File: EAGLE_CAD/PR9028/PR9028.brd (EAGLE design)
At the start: 65.9 x 66 mm, 60 parts, among them SW1 C&K_PTS645, T1 TPTP20R, T10 TPTP20R, T11 TPTP20R, T12 TPTP20R, T13 TPTP20R, T14 TPTP20R, T15 TPTP20R, T16 TPTP20R, T17 TPTP20R, T2 TPTP20R, T3 TPTP20R, T4 TPTP20R, T5 TPTP20R, T6 TPTP20R, T7 TPTP20R, T8 TPTP20R, T9 TPTP20R, U1 FMIC

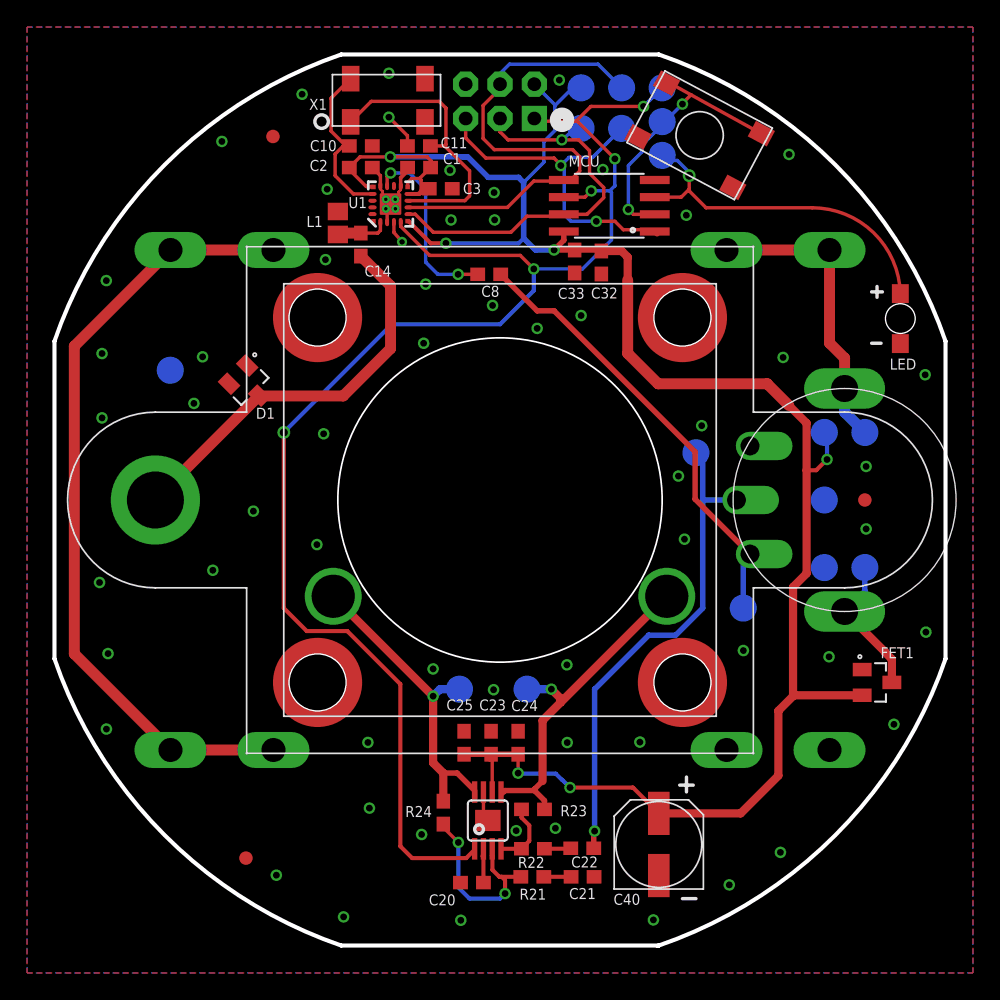
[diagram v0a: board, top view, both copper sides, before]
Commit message: started edits for pot, battery clips
bumping to PR9028. not done with my changes yet, but started.
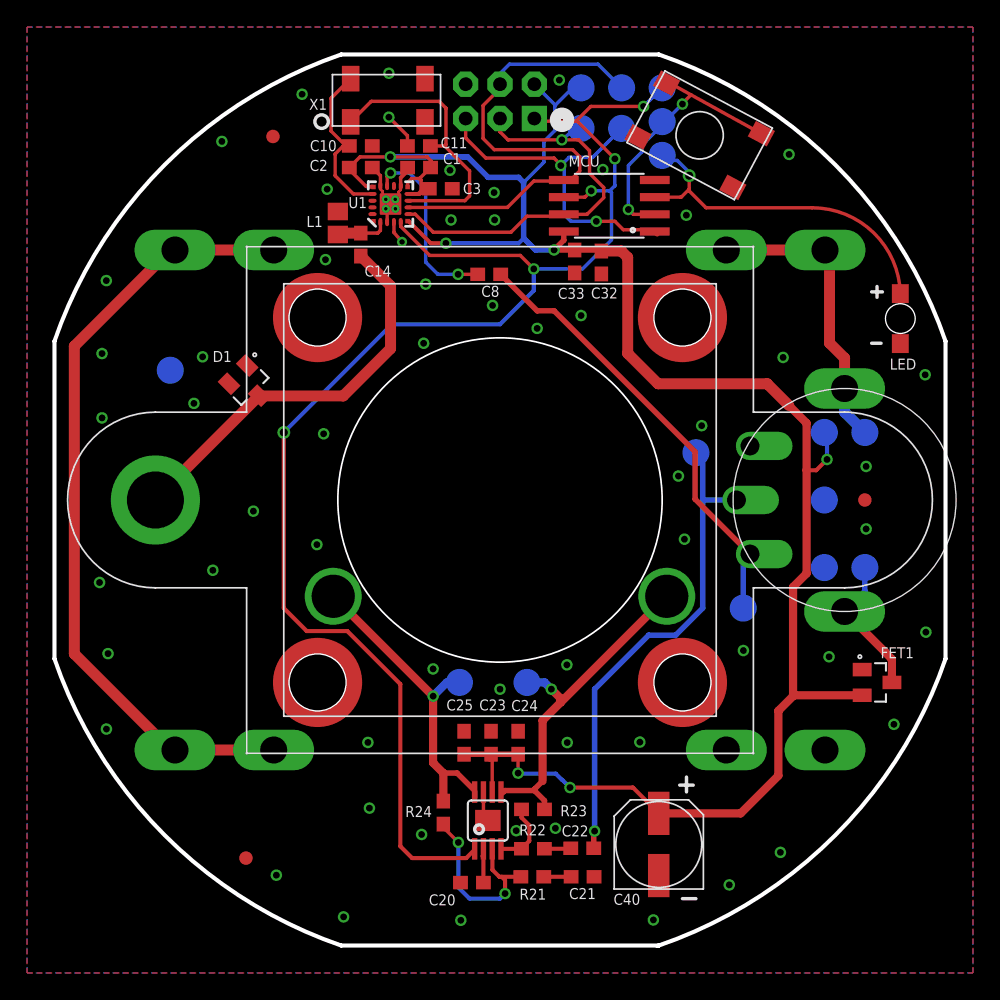
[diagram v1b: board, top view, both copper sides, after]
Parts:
- JP5, JP6: value (none) -> BK-92_MPD_AA_BATT_CLIP
- moved T6 0.50 mm to (37.0, 21.5)
- moved T7 0.50 mm to (32.0, 21.5)

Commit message: updated pot and battery clips
plus small stuff.
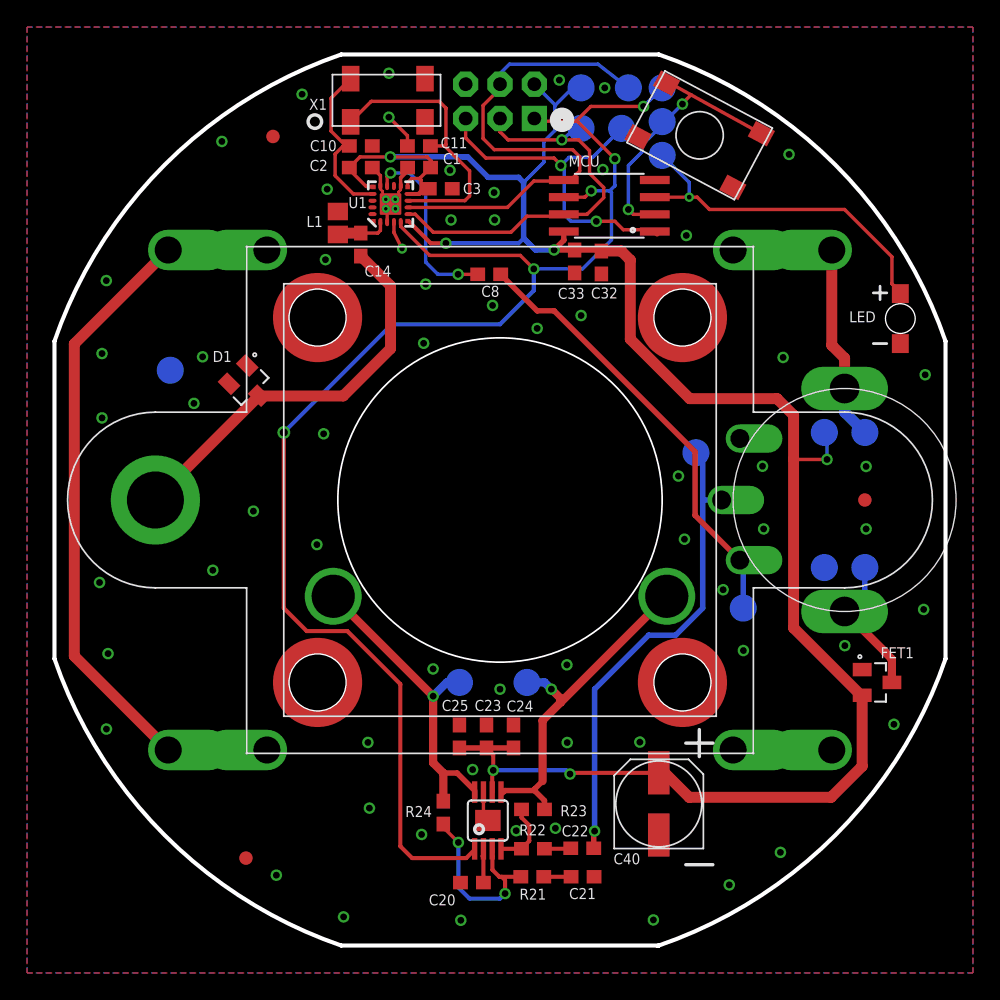
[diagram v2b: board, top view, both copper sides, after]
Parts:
- removed T3: TPTP20R, PR_Parts_Library:TP20R
- moved T2 5.00 mm to (59.0, 30.0)
- moved C40 3.00 mm to (46.8, 12.5)
- moved C23 0.57 mm to (34.0, 17.5)
- moved C24 0.57 mm to (36.0, 17.5)
- moved C25 0.57 mm to (32.0, 17.5)
- moved T13 0.50 mm to (44.5, 65.5)
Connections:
- net GND: no longer T3.TP
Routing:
- net A_OUT: track 36.5 -> 35.4 mm
- net LED/PB4: track 25.4 -> 26.5 mm
- net N$13: track 58.1 -> 57.4 mm
- net GND: track 15.1 -> 15.5 mm, vias 63 -> 67

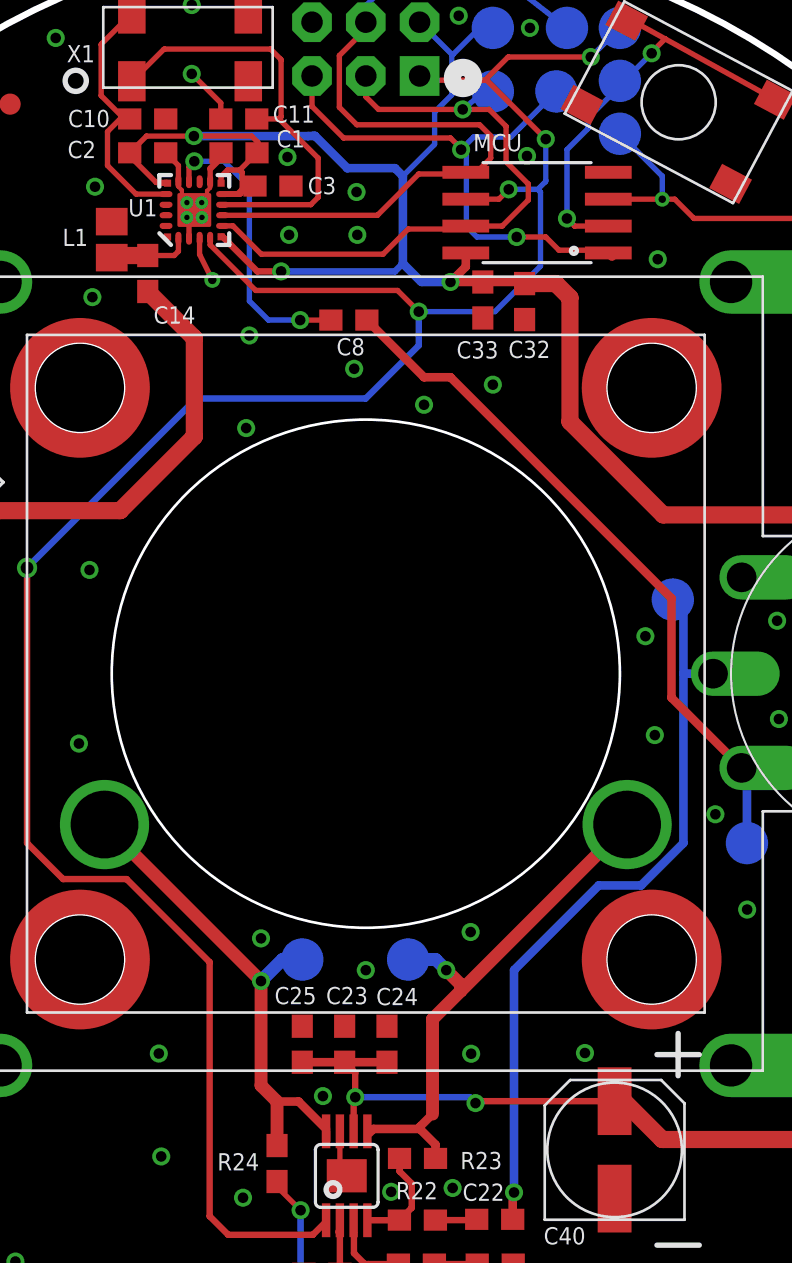
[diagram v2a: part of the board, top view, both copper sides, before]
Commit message: Added jumper footprints
Added back in 0603 footprints for jumpers or potentially ferrite beads:
-L2 near the FMIC required rerouting of the power traces to decoupling caps.
-L3 is near the AMP.
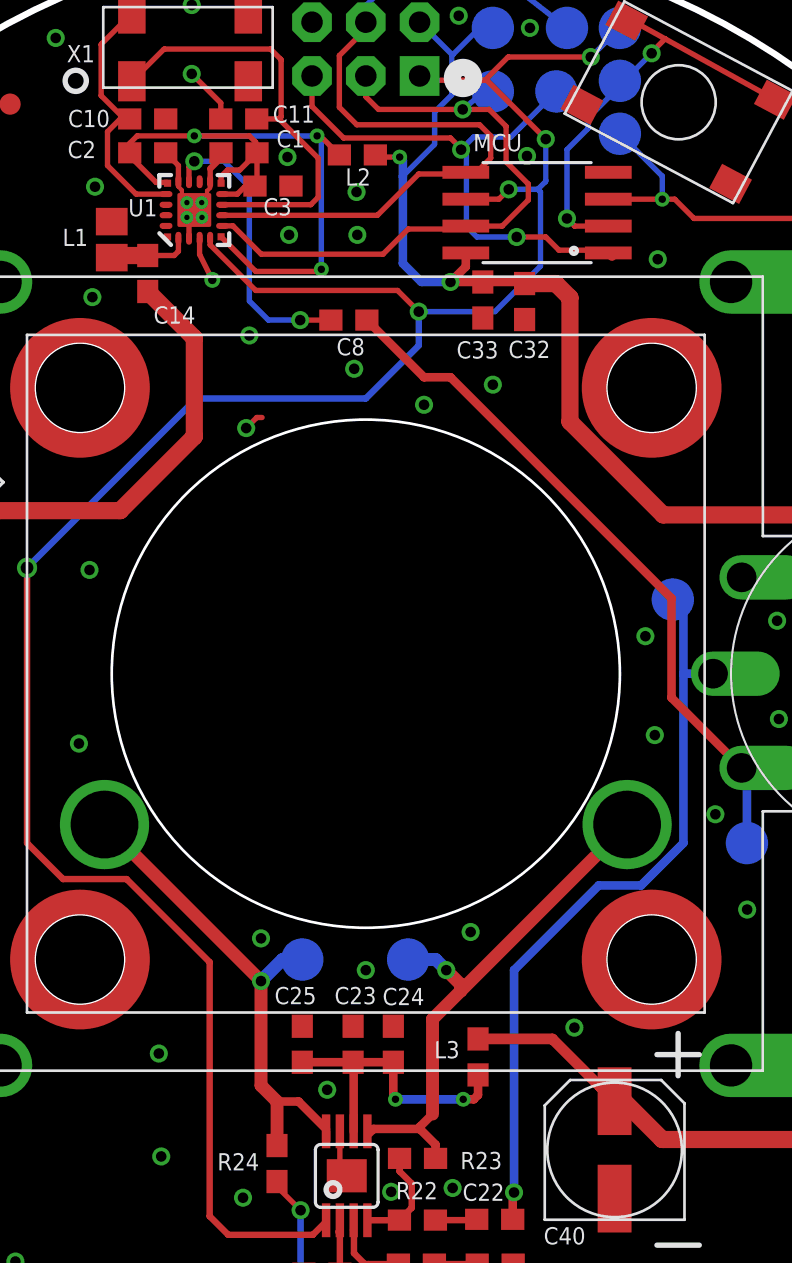
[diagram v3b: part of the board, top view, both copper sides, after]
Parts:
- added L2, L3: 2.2K @ 100Mhz, PR_Parts_Library:0603_CPL
- moved C23 0.40 mm to (34.4, 17.5)
- moved C24 0.30 mm to (36.3, 17.5)
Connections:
- new net N$4: AMP.6, C23.1, C24.1, C25.1, L3.2
- new net N$6: C1.1, C2.1, C3.1, L2.2, U1.10, U1.11, U1.16, U1.6
- net VCC: now also L2.1, L3.1; no longer AMP.6, C1.1, C2.1, C23.1, C24.1, C25.1, C3.1, U1.10, U1.11, U1.16, U1.6
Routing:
- net VCC: track 151.6 -> 106.2 mm, vias 6 -> 3
- net N$6: track 0.00 -> 34.5 mm, vias 0 -> 3
- net N$4: track 0.00 -> 14.3 mm, vias 0 -> 2
- net GND: track 15.5 -> 16.3 mm, vias 67 -> 66
- net LED/PB4: track 26.5 -> 27.0 mm

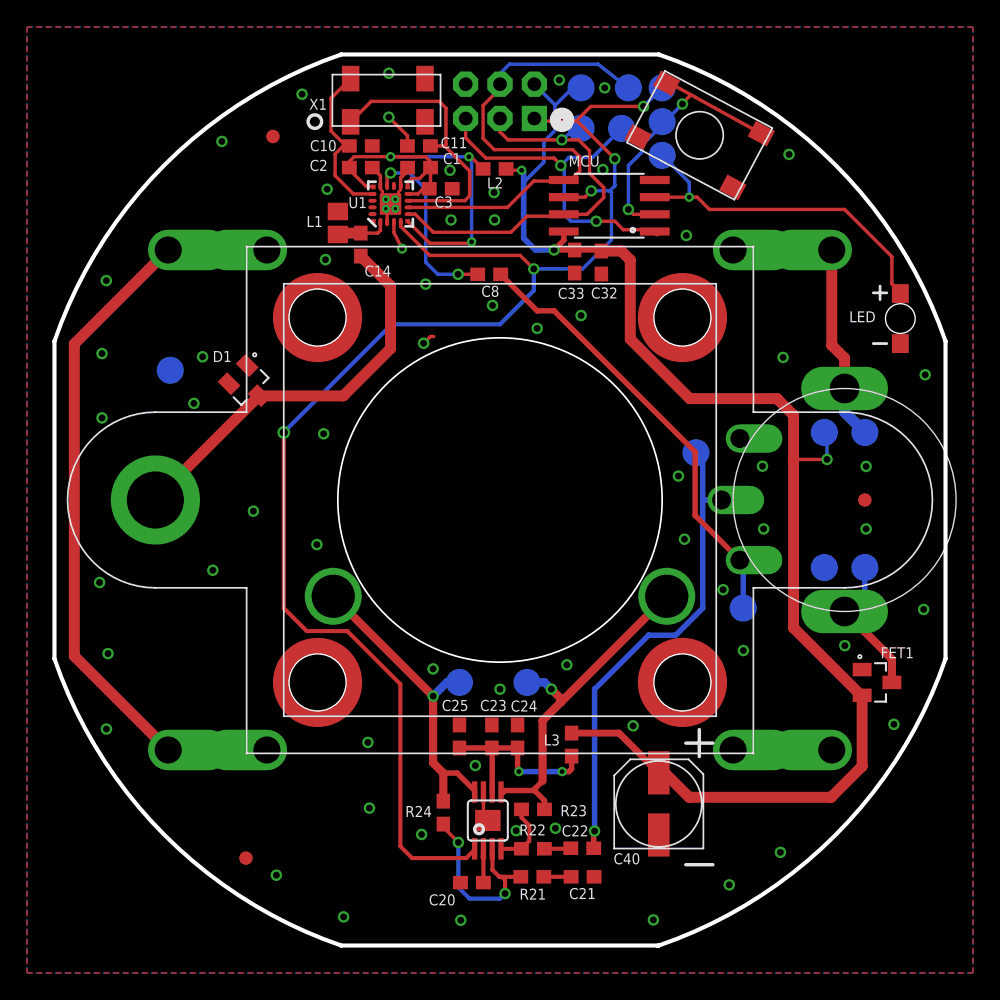
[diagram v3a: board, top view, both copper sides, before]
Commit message: PR9028 Updates
Updated Speaker PEM Nuts:
- currently designed with top and bottom smd pads
- top pad 6.6 mm bottom pad 4.72 mm, drill 4.22 mm
Updated library:
- there are now 3 PEM nut ‘devices:’ ANT, SPK, SPK_GROUND to match our
three different PEM nut uses.
- there are now 2 PEM nut ‘packages:’ ANT, SPK
Updated layout:
- minor changes to some vias
- updated logo placement and URL
Exported BOM & Gerbers
Ran DRC:
- showing errors for speaker Pem nuts & speaker pc pins. need to
confirm with WAI about plating *all* pem nut holes.
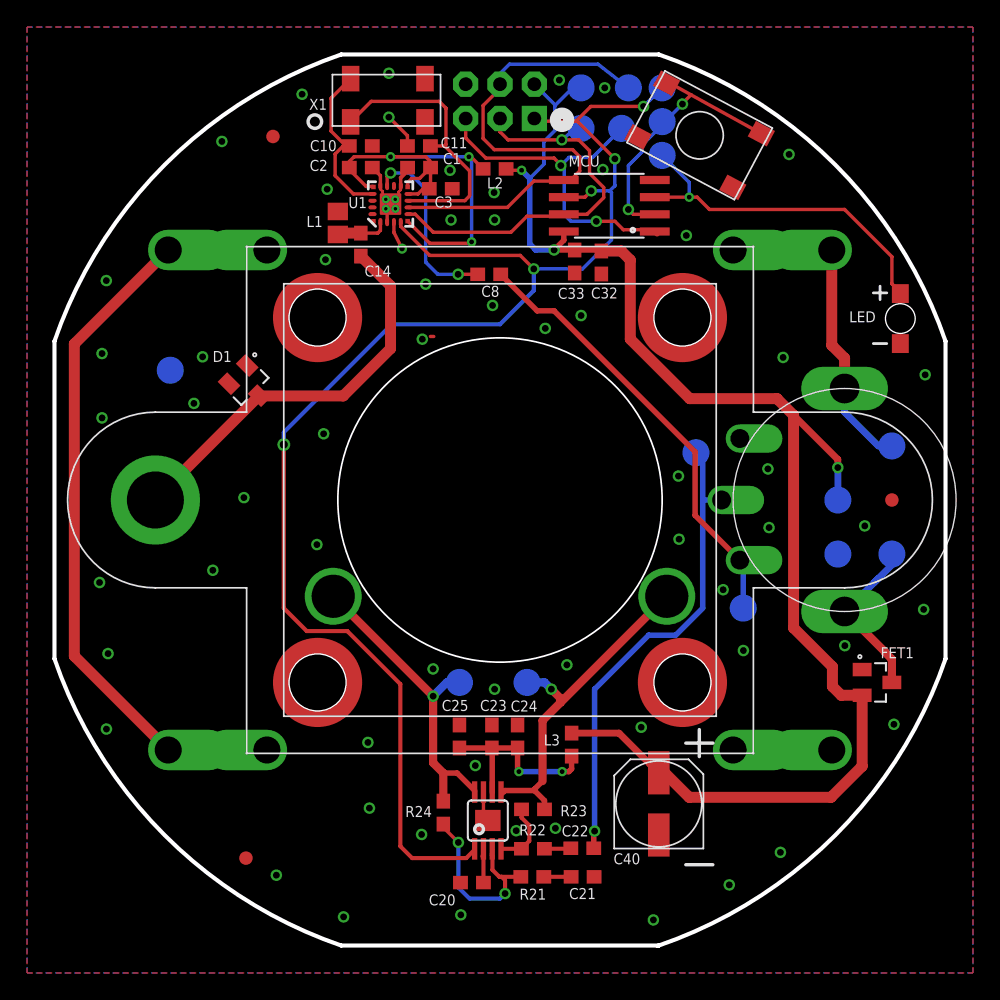
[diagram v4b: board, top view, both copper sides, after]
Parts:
- SPEAKER_PEM_1, SPEAKER_PEM_2, SPEAKER_PEM_4: value PEM_M3_ONE_SIDE -> PEM_M3_SPK; device PR_Parts_Library:PEM_M3_ONE_SIDE -> PR_Parts_Library:PEM_M3_SPK
- SPEAKER_PEM_3: value PEM_M3_ONE_SIDE_W/PIN -> PEM_M3_SPK_GROUND; device PR_Parts_Library:PEM_M3_ONE_SIDE -> PR_Parts_Library:PEM_M3_SPK
- moved T4 5.10 mm to (60.0, 35.0)
- moved T14 2.24 mm to (64.0, 31.0)
- moved T15 2.24 mm to (64.0, 39.0)
- moved MARK3 2.00 mm to (64.0, 35.0)
- moved T2 1.41 mm to (60.0, 31.0)
- moved U$1 0.40 mm to (35.0, 8.60)
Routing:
- net VCC: track 106.2 -> 110.0 mm
- net SW_OUT: track 21.8 -> 24.2 mm
- net SW_IN: track 10.6 -> 12.8 mm
- net GND: track 16.3 -> 15.6 mm, vias 66 -> 65
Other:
- board text added: "www.thepublicrad.io"
- board text removed: "The Public Radio Born in Brooklyn http://thepublicrad.io"

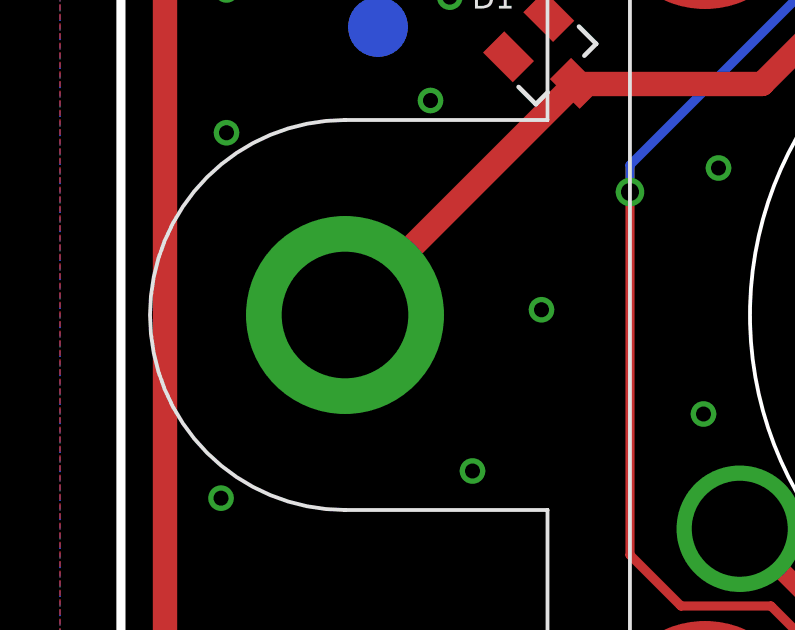
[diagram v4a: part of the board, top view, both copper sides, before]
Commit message: 9028 Updates
PEM nuts:
- Updated the antenna package to match the speaker PEM packages
(top/bottom pads)
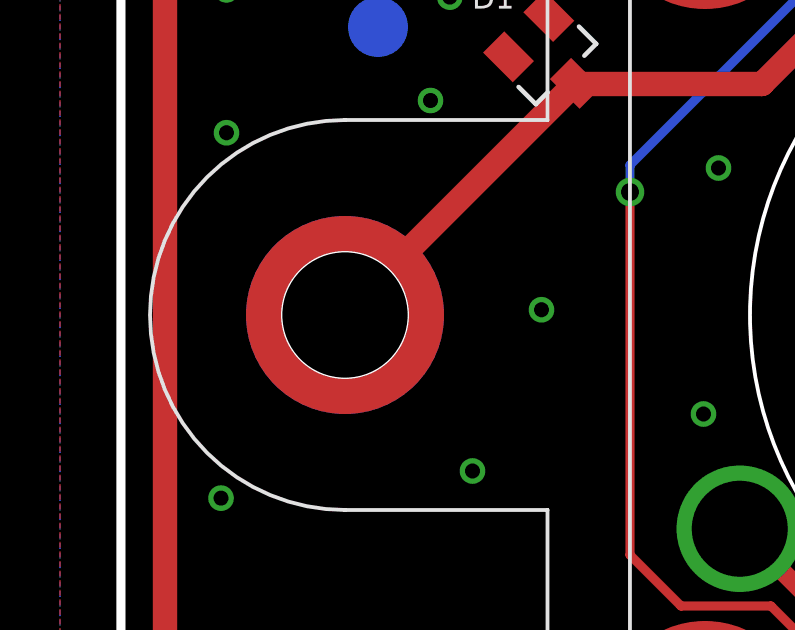
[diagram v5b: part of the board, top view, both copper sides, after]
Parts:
- ANT_MOUNT: value PEM_M3 -> PEM_M3_ANTENNA; device PR_Parts_Library:PEM_M3 -> PR_Parts_Library:PEM_M3_ANTENNA
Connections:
- net ANT: now also ANT_MOUNT.P$1; no longer ANT_MOUNT.P$2
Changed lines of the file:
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@@
 <layer number="29" name="tStop" color="7" fill="3" visible="no" active="yes"/>
 <layer number="30" name="bStop" color="7" fill="6" visible="no" active="yes"/>
-<layer number="31" name="tCream" color="7" fill="4" visible="no" active="yes"/>
+<layer number="31" name="tCream" color="7" fill="4" visible="yes" active="yes"/>
 <layer number="32" name="bCream" color="7" fill="5" visible="no" active="yes"/>
 <layer number="33" name="tFinish" color="6" fill="3" visible="no" active="yes"/>
@@
 <attribute name="VOLTAGE" value="16V" x="41.11125" y="7.11625" size="1.778" layer="27" rot="R180" display="off"/>
 </element>
-<element name="ANT_MOUNT" library="PR_Parts_Library" package="PEM_M3" value="PEM_M3" x="9.5" y="35" locked="yes" smashed="yes">
+<element name="ANT_MOUNT" library="PR_Parts_Library" package="PEM_M3_ANTENNA" value="PEM_M3_ANTENNA" x="9.5" y="35" locked="yes" smashed="yes">
 <attribute name="CENTERLINE_PN" value="PR2040" x="9.5" y="35" size="1.778" layer="27" display="off"/>
 <attribute name="MFG_PN" value="Consigned" x="9.5" y="35" size="1.778" layer="27" display="off"/>
@@
 </signal>
 <signal name="ANT" class="1">
-<contactref element="ANT_MOUNT" pad="P$2"/>
+<contactref element="ANT_MOUNT" pad="P$1"/>
 <contactref element="D1" pad="3"/>
 <contactref element="C14" pad="1"/>
